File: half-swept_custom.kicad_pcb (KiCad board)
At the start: 2 copper layers, 108.6 x 86.9 mm, 22 parts, among them J2 AudioJack4dpb, SW10 SW_Push, SW11 SW_Push, SW12 SW_Push, SW14 SW_Push, SW15 SW_Push, SW16 SW_Push, SW17 SW_Push, SW18 SW_Push, SW2 SW_Push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

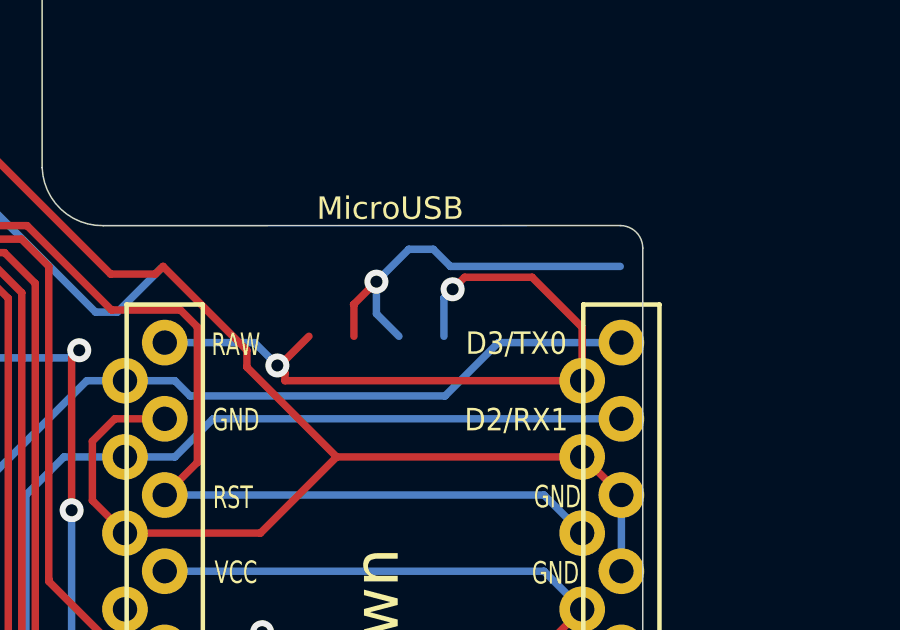
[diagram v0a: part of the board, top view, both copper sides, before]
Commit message: Remove unused power switch traces
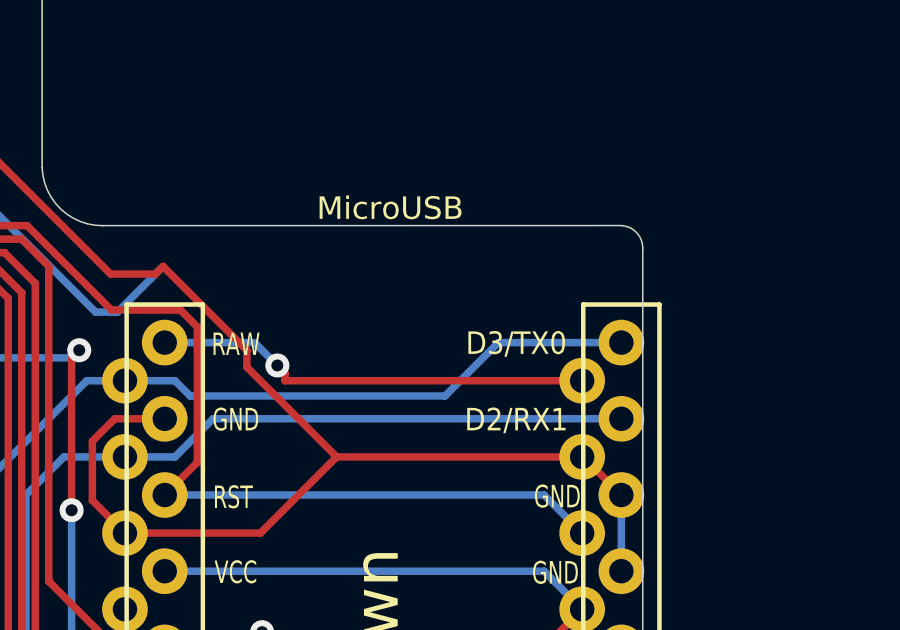
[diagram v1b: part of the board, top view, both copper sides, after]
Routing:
- net BT+_r: track 13.1 -> 0.00 mm, vias 1 -> 0
- net raw: track 24.7 -> 14.7 mm, vias 2 -> 1
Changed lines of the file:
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@@
     (thickness 1.6)
     (drawings 20)
-    (tracks 593)
+    (tracks 575)
     (zones 0)
     (modules 22)
-    (nets 24)
+    (nets 23)
   )
   (page A4)
@@
     (mod_text_size 1 1)
     (mod_text_width 0.15)
-    (pad_size 0.9 1.25)
-    (pad_drill 0)
+    (pad_size 2 2)
+    (pad_drill 1.3)
     (pad_to_mask_clearance 0)
     (aux_axis_origin 0 0)
@@
   (net 21 Switch17)
   (net 22 raw)
-  (net 23 BT+_r)
   (net_class Default "This is the default net class."
     (clearance 0.2)
@@
     (uvia_dia 0.3)
     (uvia_drill 0.1)
-    (add_net BT+_r)
     (add_net Switch1)
     (add_net Switch10)
@@
   (segment (start 121.4484 71.374) (end 121.294195 71.528205) (width 0.25) (layer F.Cu) (net 21))
   (segment (start 118.618 77.216) (end 119.888 75.946) (width 0.25) (layer F.Cu) (net 21))
-  (via (at 115.824 41.656) (size 0.8) (drill 0.4) (layers F.Cu B.Cu) (net 22))
-  (segment (start 115.534 41.946) (end 115.824 41.656) (width 0.25) (layer B.Cu) (net 22))
-  (segment (start 115.534 43.223) (end 115.534 41.946) (width 0.25) (layer B.Cu) (net 22))
   (segment (start 110.236 44.704) (end 110.236 44.45) (width 0.25) (layer F.Cu) (net 22))
   (segment (start 110.236 44.704) (end 120.142 44.704) (width 0.25) (layer F.Cu) (net 22))
@@
   (segment (start 109.22 43.434) (end 109.982 44.196) (width 0.25) (layer B.Cu) (net 22))
   (segment (start 106.2284 43.434) (end 109.22 43.434) (width 0.25) (layer B.Cu) (net 22))
-  (segment (start 110.061 44.196) (end 111.034 43.223) (width 0.25) (layer F.Cu) (net 22))
   (segment (start 109.982 44.196) (end 110.061 44.196) (width 0.25) (layer F.Cu) (net 22))
-  (segment (start 116.223999 41.256001) (end 118.472001 41.256001) (width 0.25) (layer F.Cu) (net 22))
-  (segment (start 115.824 41.656) (end 116.223999 41.256001) (width 0.25) (layer F.Cu) (net 22))
-  (segment (start 120.142 42.926) (end 120.142 44.704) (width 0.25) (layer F.Cu) (net 22))
-  (segment (start 118.472001 41.256001) (end 120.142 42.926) (width 0.25) (layer F.Cu) (net 22))
-  (via (at 113.284 41.402) (size 0.8) (drill 0.4) (layers F.Cu B.Cu) (net 23))
-  (segment (start 113.284 41.402) (end 112.522 42.164) (width 0.25) (layer F.Cu) (net 23))
-  (segment (start 112.534 42.176) (end 112.534 43.223) (width 0.25) (layer F.Cu) (net 23))
-  (segment (start 112.522 42.164) (end 112.534 42.176) (width 0.25) (layer F.Cu) (net 23))
-  (segment (start 114.363001 40.322999) (end 113.284 41.402) (width 0.25) (layer B.Cu) (net 23))
-  (segment (start 115.751002 40.894) (end 115.180001 40.322999) (width 0.25) (layer B.Cu) (net 23))
-  (segment (start 115.180001 40.322999) (end 114.363001 40.322999) (width 0.25) (layer B.Cu) (net 23))
-  (segment (start 121.412 40.894) (end 115.751002 40.894) (width 0.25) (layer B.Cu) (net 23))
-  (segment (start 113.284 42.473) (end 114.034 43.223) (width 0.25) (layer B.Cu) (net 23))
-  (segment (start 113.284 41.402) (end 113.284 42.473) (width 0.25) (layer B.Cu) (net 23))
   (zone (net 1) (net_name gnd) (layer F.Cu) (hatch edge 0.508)
     (connect_pads (clearance 0.508))
